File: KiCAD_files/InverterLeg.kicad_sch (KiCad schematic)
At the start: 74 parts, among them U601 AMC1100DUB, U603 UCC21222DR, U605 ACS730KLCTR-20AB

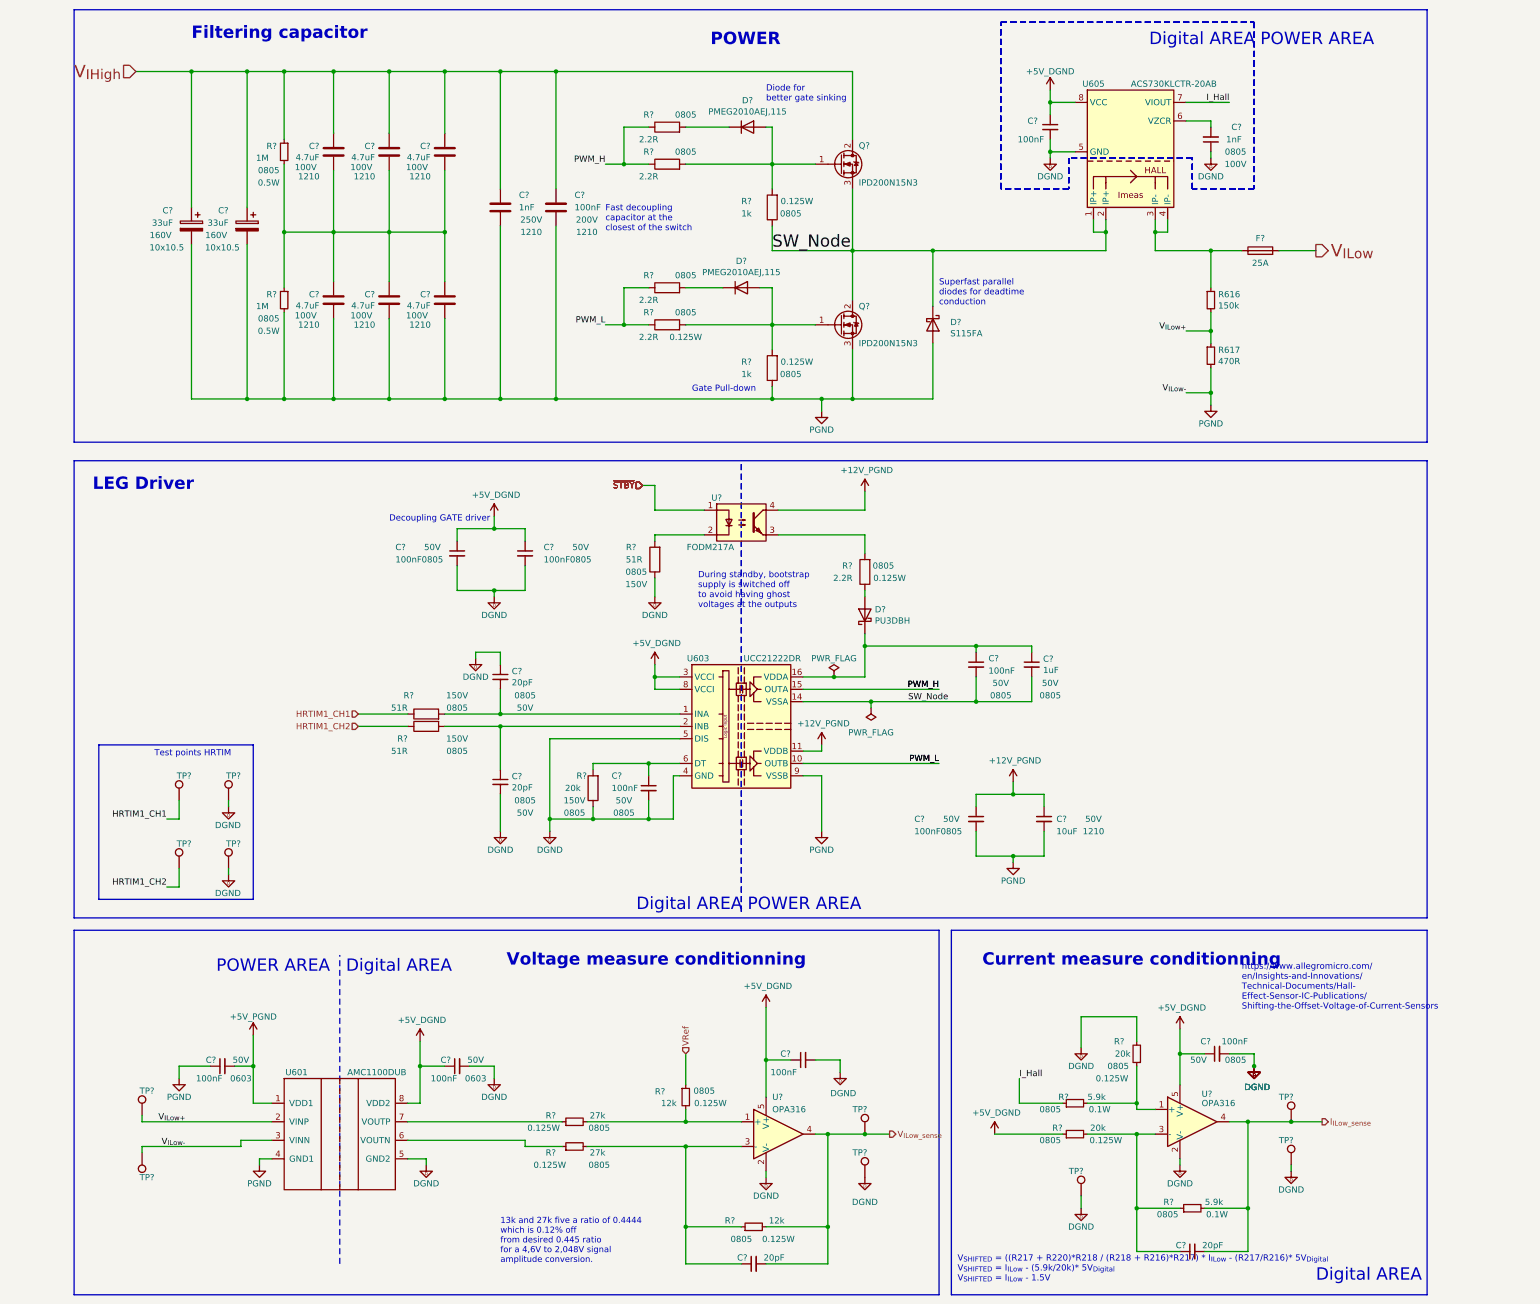
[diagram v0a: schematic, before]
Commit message: Added ERC rules for galvanic isolation. Modified SPIN pinout.
Signed-off-by: Jean Alinei <jean.alinei@laas.fr>
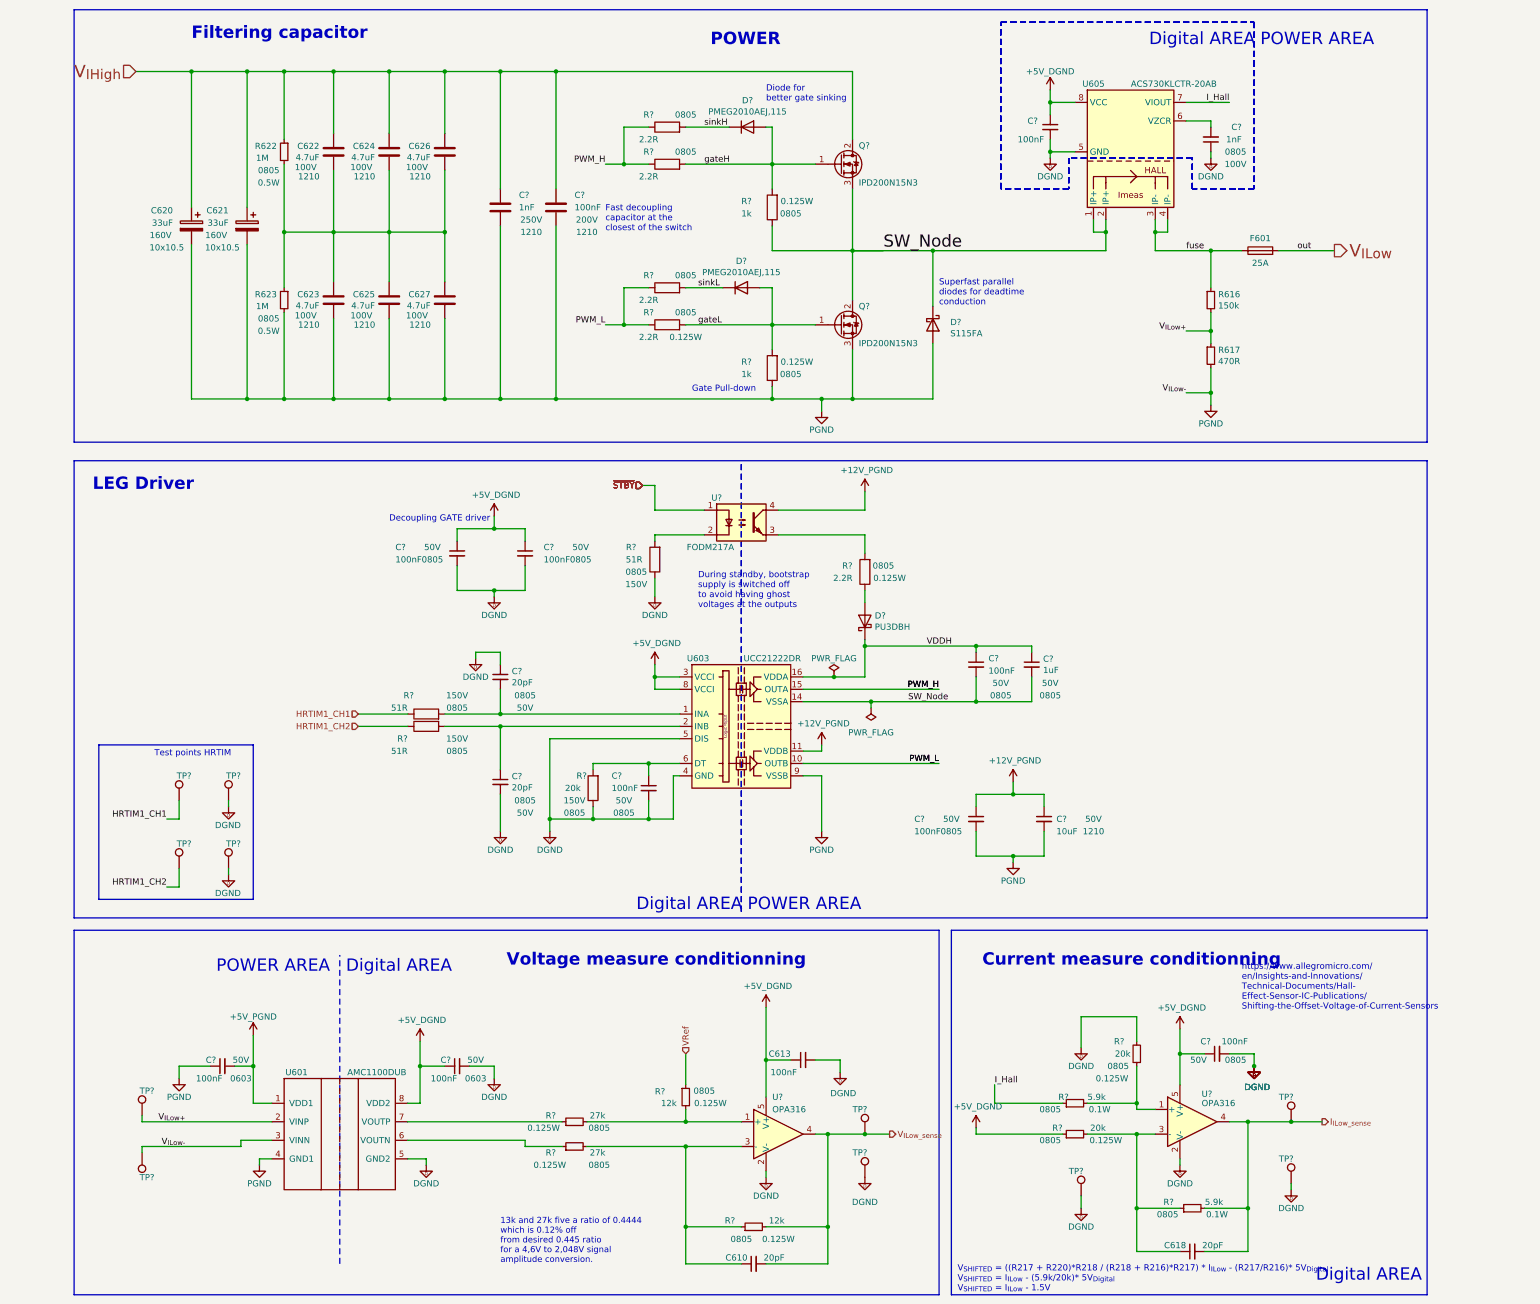
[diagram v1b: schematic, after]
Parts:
- gave numbers to parts that had none: 14
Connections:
- net sinkL: now reaches D?.1 (K), R?.2
- net VDDH: now reaches C?.1, C?.1, D?.1 (K), U603.16 (VDDA)
- net gateL: now reaches D?.2 (A), Q?.1 (G), R?.2, R?.2
- net sinkH: now reaches D?.1 (K), R?.2
- net gateH: now reaches D?.2 (A), Q?.1 (G), R?.2, R?.2
- net fuse: now reaches F601.1, R616.1, U605.3 (IP-), U605.4 (IP-)
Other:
- moved on the sheet: D?, TP?
